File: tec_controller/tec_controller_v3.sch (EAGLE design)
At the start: 24 parts, among them IC1 LM358N, Q1 IRF512, Q2 IRF512

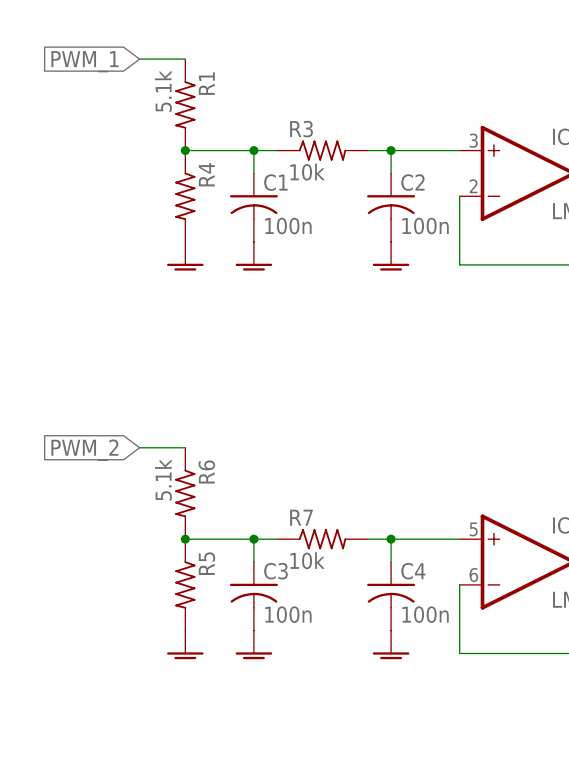
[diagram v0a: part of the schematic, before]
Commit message: adjustments to tec controller board and schematic
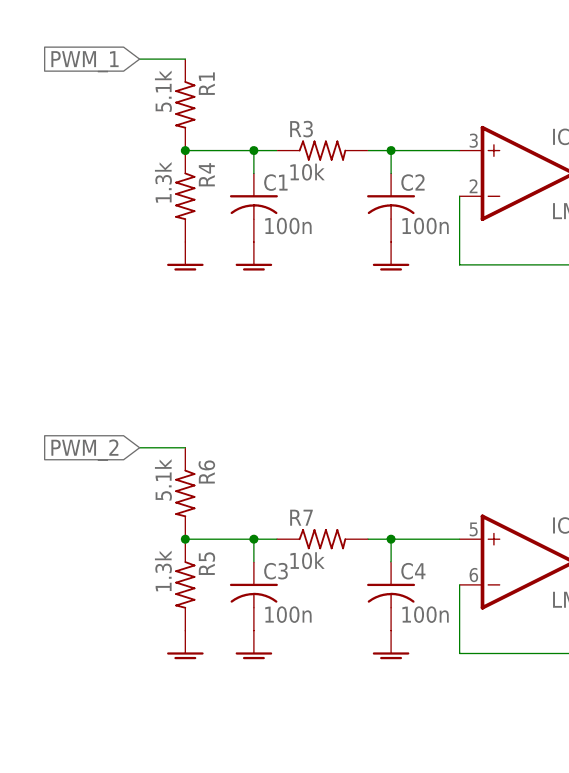
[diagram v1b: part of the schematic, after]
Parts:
- R4, R5: value (none) -> 1.3k
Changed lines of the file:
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@@
 <part name="GND14" library="supply1" deviceset="GNDA" device=""/>
 <part name="CONTROL" library="SparkFun-Connectors" deviceset="M04" device="POLAR"/>
-<part name="R4" library="rcl" deviceset="R-US_" device="M0805"/>
+<part name="R4" library="rcl" deviceset="R-US_" device="M0805" value="1.3k"/>
 <part name="GND6" library="supply1" deviceset="GNDA" device=""/>
-<part name="R5" library="rcl" deviceset="R-US_" device="M0805"/>
+<part name="R5" library="rcl" deviceset="R-US_" device="M0805" value="1.3k"/>
 <part name="GND9" library="supply1" deviceset="GNDA" device=""/>
 <part name="IC1" library="linear" deviceset="LM358" device="N"/>
